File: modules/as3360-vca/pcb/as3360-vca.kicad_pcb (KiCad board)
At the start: 2 copper layers, 38.4 x 100.5 mm, 35 parts, among them J1 Thonkiconn SM, J2 Thonkiconn SM, J3 Thonkiconn SM, J4 Thonkiconn SM, J5 IDC Header 2x8, J6 Thonkiconn SM, J7 Thonkiconn SM, U1 TL074, U2 AS3360

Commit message: modules: as3360-vca: upgrade to kicad 6
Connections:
- J3 pad TN: (no net) -> unconnected-(J3-PadTN)
- J4 pad TN: (no net) -> unconnected-(J4-PadTN)
- J5 pad 11: (no net) -> unconnected-(J5-Pad11)
- J5 pad 12: (no net) -> unconnected-(J5-Pad12)
- J5 pad 13: (no net) -> unconnected-(J5-Pad13)
- J5 pad 14: (no net) -> unconnected-(J5-Pad14)
- J5 pad 15: (no net) -> unconnected-(J5-Pad15)
- J5 pad 16: (no net) -> unconnected-(J5-Pad16)
- J6 pad TN: (no net) -> unconnected-(J6-PadTN)
- J7 pad TN: (no net) -> unconnected-(J7-PadTN)
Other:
- net class Default removed

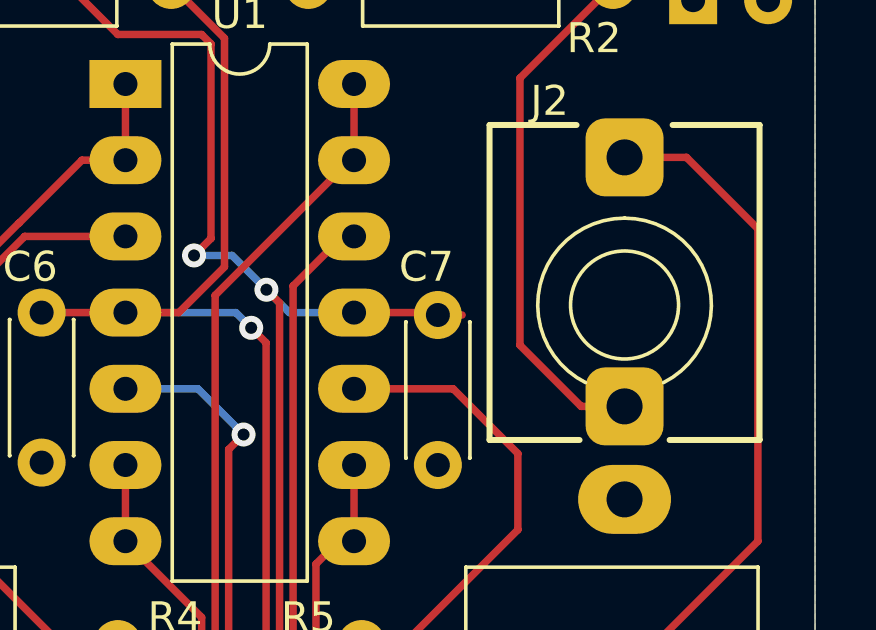
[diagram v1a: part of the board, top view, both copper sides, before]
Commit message: modules: as3360-vca: remove unconnected nets
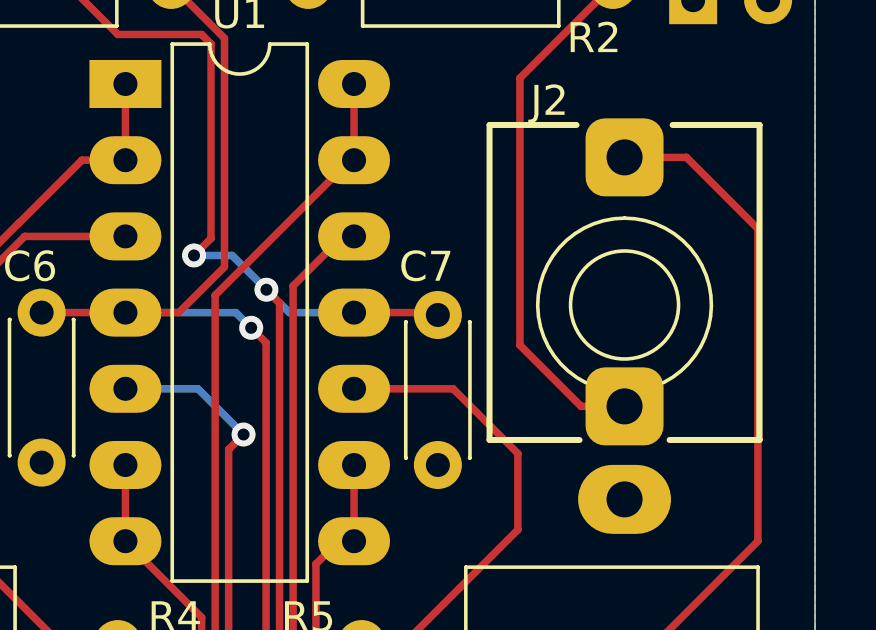
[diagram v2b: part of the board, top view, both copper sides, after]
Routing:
- net -12V: track 94.0 -> 93.2 mm
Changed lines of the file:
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@@
   )
   (segment (start 120.142 119.126) (end 120.142 116.459) (width 0.25) (layer "F.Cu") (net 2))
-  (segment (start 116.586 73.787) (end 116.586 73.787) (width 0.25) (layer "F.Cu") (net 3))
-  (segment (start 116.713 100.838) (end 116.713 100.838) (width 0.25) (layer "F.Cu") (net 3))
   (segment (start 131.318 56.261) (end 127.381 52.324) (width 0.25) (layer "F.Cu") (net 3))
   (segment (start 127.381 52.324) (end 119.126 52.324) (width 0.25) (layer "F.Cu") (net 3))
@@
   (segment (start 117.094 101.219) (end 116.713 100.838) (width 0.25) (layer "B.Cu") (net 3))
   (segment (start 120.142 101.219) (end 117.094 101.219) (width 0.25) (layer "B.Cu") (net 3))
-  (segment (start 117.094 72.517) (end 117.094 72.517) (width 0.25) (layer "F.Cu") (net 4))
   (segment (start 116.3955 116.3955) (end 116.332 116.459) (width 0.25) (layer "F.Cu") (net 4))
-  (segment (start 114.681 71.374) (end 114.681 71.374) (width 0.25) (layer "F.Cu") (net 4))
   (segment (start 117.53299 72.95599) (end 117.532991 103.183401) (width 0.25) (layer "F.Cu") (net 4))
   (segment (start 120.015 73.279) (end 122.729 73.279) (width 0.25) (layer "F.Cu") (net 4))
@@
   (segment (start 104.648 57.023) (end 101.052 60.619) (width 0.25) (layer "F.Cu") (net 4))
   (segment (start 112.141 64.008) (end 114.93359 64.008) (width 0.25) (layer "F.Cu") (net 4))
-  (segment (start 123.618 73.359) (end 122.809 73.359) (width 0.25) (layer "F.Cu") (net 4))
   (segment (start 107.315 57.023) (end 107.315 59.182) (width 0.25) (layer "F.Cu") (net 4))
   (segment (start 107.315 59.182) (end 112.141 64.008) (width 0.25) (layer "F.Cu") (net 4))
@@
   (segment (start 120.142 113.919) (end 121.793 113.919) (width 0.25) (layer "F.Cu") (net 21))
   (segment (start 121.793 113.919) (end 123.317 115.443) (width 0.25) (layer "F.Cu") (net 21))
-  (segment (start 116.332 77.343) (end 116.332 77.343) (width 0.25) (layer "F.Cu") (net 22))
-  (segment (start 116.205 103.759) (end 116.205 103.759) (width 0.25) (layer "F.Cu") (net 22))
   (segment (start 115.83502 103.38902) (end 116.205 103.759) (width 0.25) (layer "F.Cu") (net 22))
   (segment (start 111.125 103.759) (end 109.347 101.981) (width 0.25) (layer "F.Cu") (net 22))

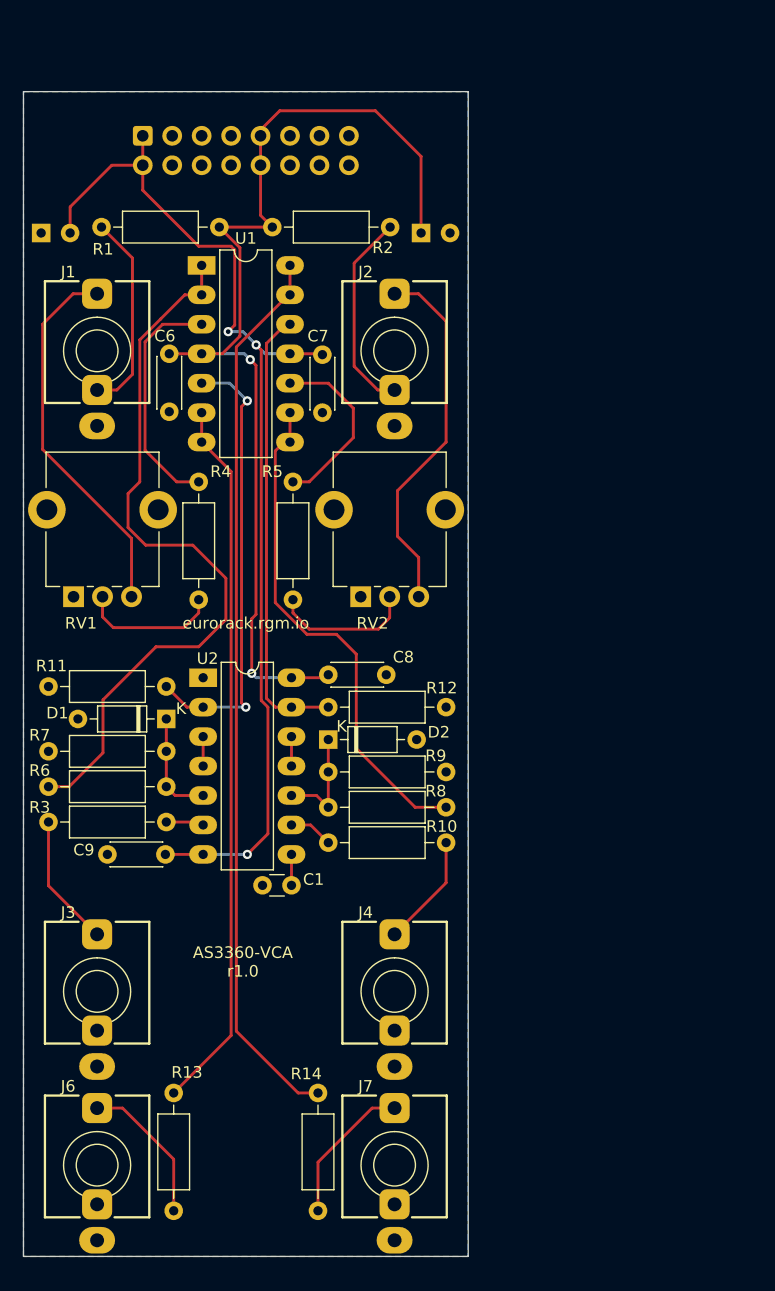
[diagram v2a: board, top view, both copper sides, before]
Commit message: modules: as3360-vca: new revision 1.1
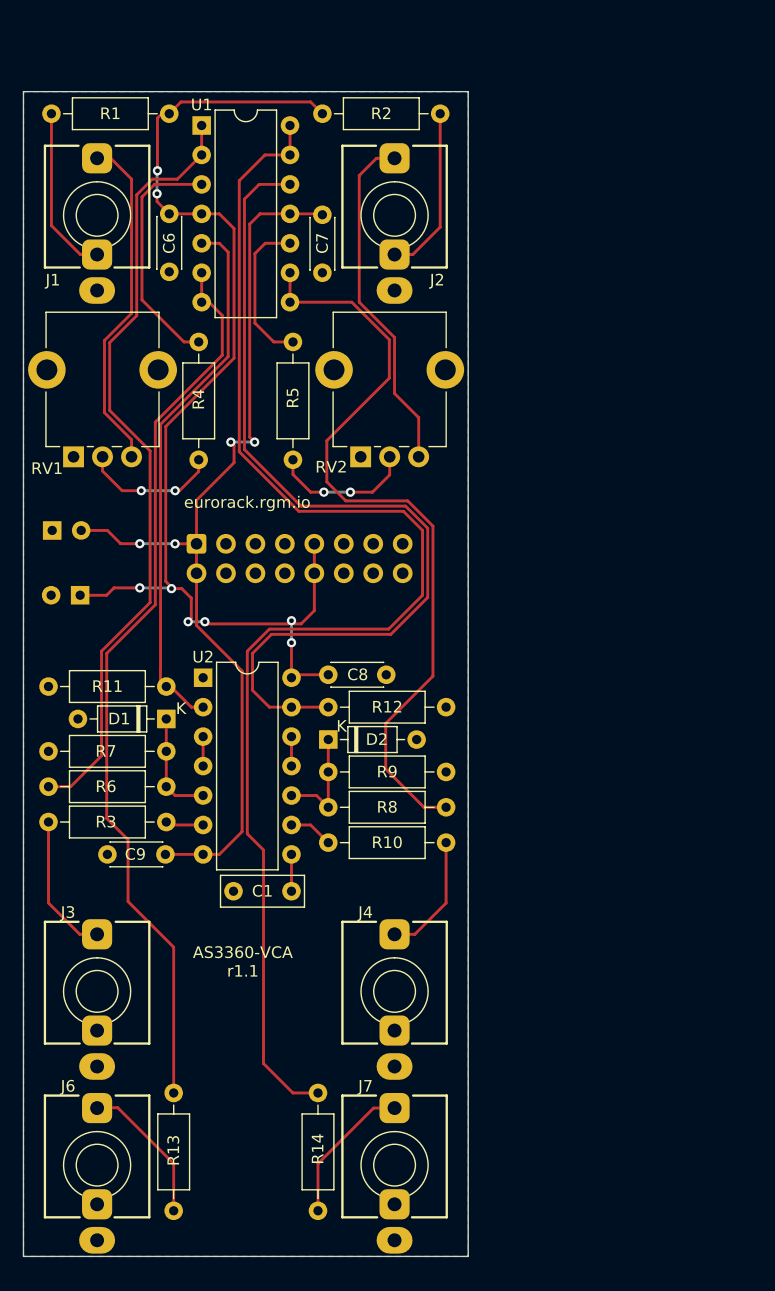
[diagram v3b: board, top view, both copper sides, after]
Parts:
- C1: footprint Capacitor_THT:C_Disc_D3.0mm_W1.6mm_P2.50mm -> Capacitor_THT:C_Rect_L7.0mm_W2.5mm_P5.00mm
- U1, U2: footprint Package_DIP:DIP-14_W7.62mm_LongPads -> Package_DIP:DIP-14_W7.62mm
- moved C2 42.9 mm to (101.9, 94.1), turned to 180 degrees
- moved J5 35.5 mm to (112.0, 89.7)
- moved C3 25.7 mm to (99.5, 88.5)
- moved U1 12.1 mm to (112.4, 53.6)
- moved C6 12.1 mm to (109.6, 61.2)
- moved C7 12.1 mm to (122.8, 66.3)
- moved R4 12.1 mm to (112.1, 72.3)
- moved R5 12.1 mm to (120.3, 72.3)
- moved RV1 12.1 mm to (101.3, 82.2)
- moved RV2 12.1 mm to (126.1, 82.2)
- moved J1 11.7 mm to (103.4, 61.3)
- moved J2 11.7 mm to (129.0, 61.3)
- moved R1 10.7 mm to (99.4, 52.6)
- moved R2 10.7 mm to (133.0, 52.6)
- moved C1 0.51 mm to (120.1, 119.6)
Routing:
- net IO2: track 39.0 -> 78.1 mm
- net Net-(R14-Pad2): track 77.3 -> 114.4 mm
- net Net-(R8-Pad2): track 44.0 -> 66.9 mm
- net Net-(R13-Pad2): track 61.8 -> 78.4 mm
- net -12V: track 93.2 -> 82.2 mm, vias 3 -> 4
- net +12V: track 91.7 -> 101.7 mm, vias 2 -> 8
- net IO1: track 38.9 -> 46.6 mm, vias 2 -> 0
- net Net-(R6-Pad2): track 63.9 -> 67.8 mm
- net Net-(J2-PadTN): track 17.6 -> 14.7 mm
- net Net-(J1-PadT): track 32.5 -> 29.6 mm
- net Net-(J1-PadTN): track 17.4 -> 14.6 mm
- net Net-(R5-Pad1): track 15.7 -> 13.3 mm
- net Net-(J2-PadT): track 31.7 -> 30.0 mm
- net Net-(J4-PadT): track 9.75 -> 10.8 mm
- net Net-(J3-PadT): track 11.4 -> 12.3 mm
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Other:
- board text added: "AS3360-VCA r1.1"
- board text removed: "AS3360-VCA r1.0"

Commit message: modules: as3360-vca: revision A (redesign)
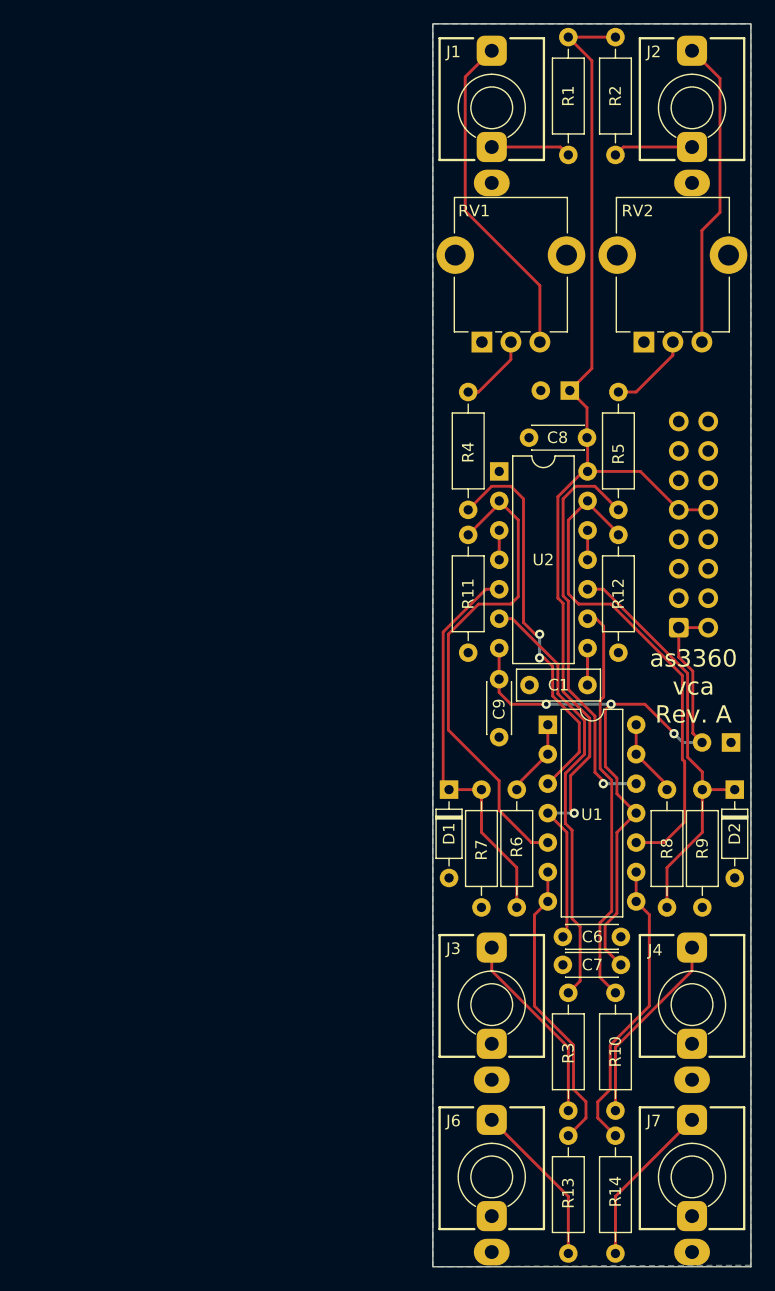
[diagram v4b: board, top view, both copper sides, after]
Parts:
- added REF**: Eurorack_PCB_6HP, eurorack:Eurorack_PCB_6HP, F.Cu at (146.1, 98.4)
- J5: value IDC Header 2x8 -> Eurorack PSU; footprint Connector_IDC:IDC-Header_2x08_P2.54mm_Vertical -> eurorack:IDC-Header_2x08_P2.54mm_Vertical
- moved REF** 80.8 mm to (146.1, 51.1)
- moved C6 71.0 mm to (143.6, 123.6), turned to 0 degrees
- moved C7 63.2 mm to (143.6, 126.0), turned to 0 degrees
- moved C3 61.3 mm to (158.1, 106.8), turned to 180 degrees
- moved U1 59.7 mm to (142.2, 105.3)
- moved C2 45.8 mm to (144.1, 76.5)
- moved R1 44.7 mm to (144.0, 56.1), turned to 90 degrees
- moved J5 42.2 mm to (153.5, 96.9), turned to 0 degrees
- moved R7 39.7 mm to (136.5, 121.0), turned to 90 degrees
- moved R3 37.7 mm to (144.0, 128.4), turned to -90 degrees
- moved RV1 36.6 mm to (136.6, 72.3)
- moved D2 35.3 mm to (158.4, 110.9), turned to -90 degrees
- moved J1 35.3 mm to (137.4, 52.1)
- moved C9 35.3 mm to (138.0, 106.3), turned to 90 degrees
- moved R13 34.2 mm to (144.0, 150.9)
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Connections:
- U1 pad 10: Net-(R5-Pad1) -> IO2
- U1 pad 12: IO2 -> Net-(R5-Pad1)
- U1 pad 13: Net-(R14-Pad2) -> Net-(R8-Pad2)
- U1 pad 14: Net-(R14-Pad2) -> Net-(R8-Pad2)
- U1 pad 8: Net-(R8-Pad2) -> Net-(R14-Pad2)
- U1 pad 9: Net-(R8-Pad2) -> Net-(R14-Pad2)
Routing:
- net Net-(R14-Pad2): track 114.4 -> 25.7 mm
- net Net-(R6-Pad2): track 67.8 -> 6.70 mm
- net Net-(R8-Pad2): track 66.9 -> 6.69 mm
- net Net-(R13-Pad2): track 78.4 -> 25.7 mm
- net IO2: track 78.1 -> 43.1 mm
- net II1: track 3.28 -> 37.6 mm
- net II2: track 3.81 -> 34.8 mm
- net VC2: track 9.44 -> 36.4 mm
- net VC1: track 9.33 -> 34.4 mm
- net Net-(R5-Pad1): track 13.3 -> 34.9 mm, vias 0 -> 1
- net -12V: track 82.2 -> 61.9 mm, vias 4 -> 3
- net Net-(R4-Pad1): track 20.9 -> 34.2 mm, vias 0 -> 2
- net Net-(J2-PadTN): track 14.7 -> 6.89 mm
- net Net-(J1-PadTN): track 14.6 -> 6.89 mm
- net Net-(J4-PadT): track 10.8 -> 16.8 mm
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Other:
- board size 38.4 x 100.5 mm -> 27.4 x 107.2 mm
- board text added: "as3360 vca Rev. A"
- board text removed: "AS3360-VCA r1.1"
